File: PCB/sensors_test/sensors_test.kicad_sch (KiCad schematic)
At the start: 16 parts, among them J1 USB4125-GF-A, U1 MIC5219-3.3YM5

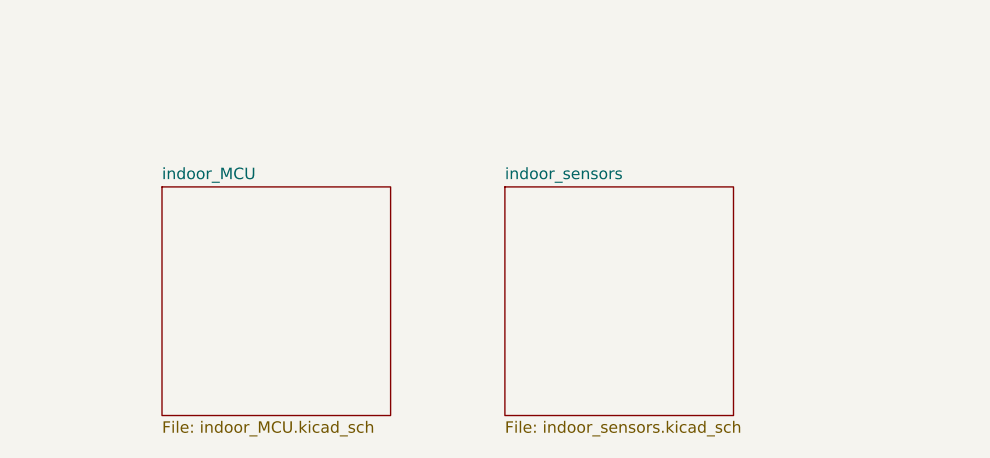
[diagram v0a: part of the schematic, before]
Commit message: Renamed PCB test project
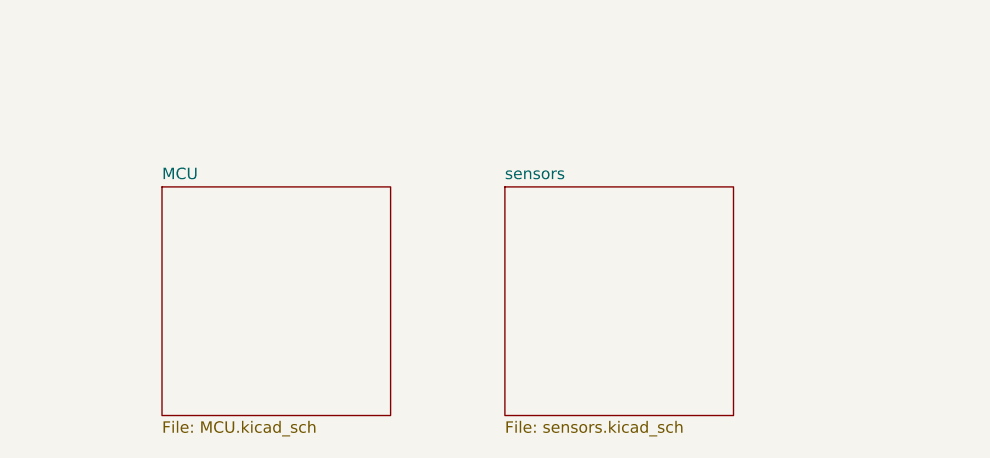
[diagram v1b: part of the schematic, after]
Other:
- sheet indoor_MCU renamed MCU
- sheet indoor_sensors renamed sensors
- sheet MCU: file indoor_MCU.kicad_sch -> MCU.kicad_sch
- sheet sensors: file indoor_sensors.kicad_sch -> sensors.kicad_sch
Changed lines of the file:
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@@
 			(color 0 0 0 0.0000)
 		)
-		(property "Sheetname" "indoor_MCU"
+		(property "Sheetname" "MCU"
 			(at 165.1 88.1884 0)
 			(effects
@@
 			)
 		)
-		(property "Sheetfile" "indoor_MCU.kicad_sch"
+		(property "Sheetfile" "MCU.kicad_sch"
 			(at 165.1 114.8846 0)
 			(effects
@@
 		)
 		(instances
-			(project "sensors_indoor"
+			(project "sensors_test"
 				(path "/09bb465b-75b9-463f-b128-e813d3269ff6"
 					(page "2")
@@
 			(color 0 0 0 0.0000)
 		)
-		(property "Sheetname" "indoor_sensors"
+		(property "Sheetname" "sensors"
 			(at 203.2 88.1884 0)
 			(effects
@@
 			)
 		)
-		(property "Sheetfile" "indoor_sensors.kicad_sch"
+		(property "Sheetfile" "sensors.kicad_sch"
 			(at 203.2 114.8846 0)
 			(effects
@@
 		)
 		(instances
-			(project "sensors_indoor"
+			(project "sensors_test"
 				(path "/09bb465b-75b9-463f-b128-e813d3269ff6"
 					(page "3")
